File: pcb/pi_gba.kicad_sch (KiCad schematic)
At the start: 22 parts, among them SW1 EG1206A, SW10 L1, SW11 R1, SW12 Start, SW13 Select, SW14 L2, SW15 R2, SW16 Menu, SW2 Left, SW3 Down, SW4 Up, SW5 Right, SW6 Y, SW7 X, SW8 B, SW9 A, U1 RPI_Zero2W, U2 ER-TFTM035-6, U3 Powerboost_1000C

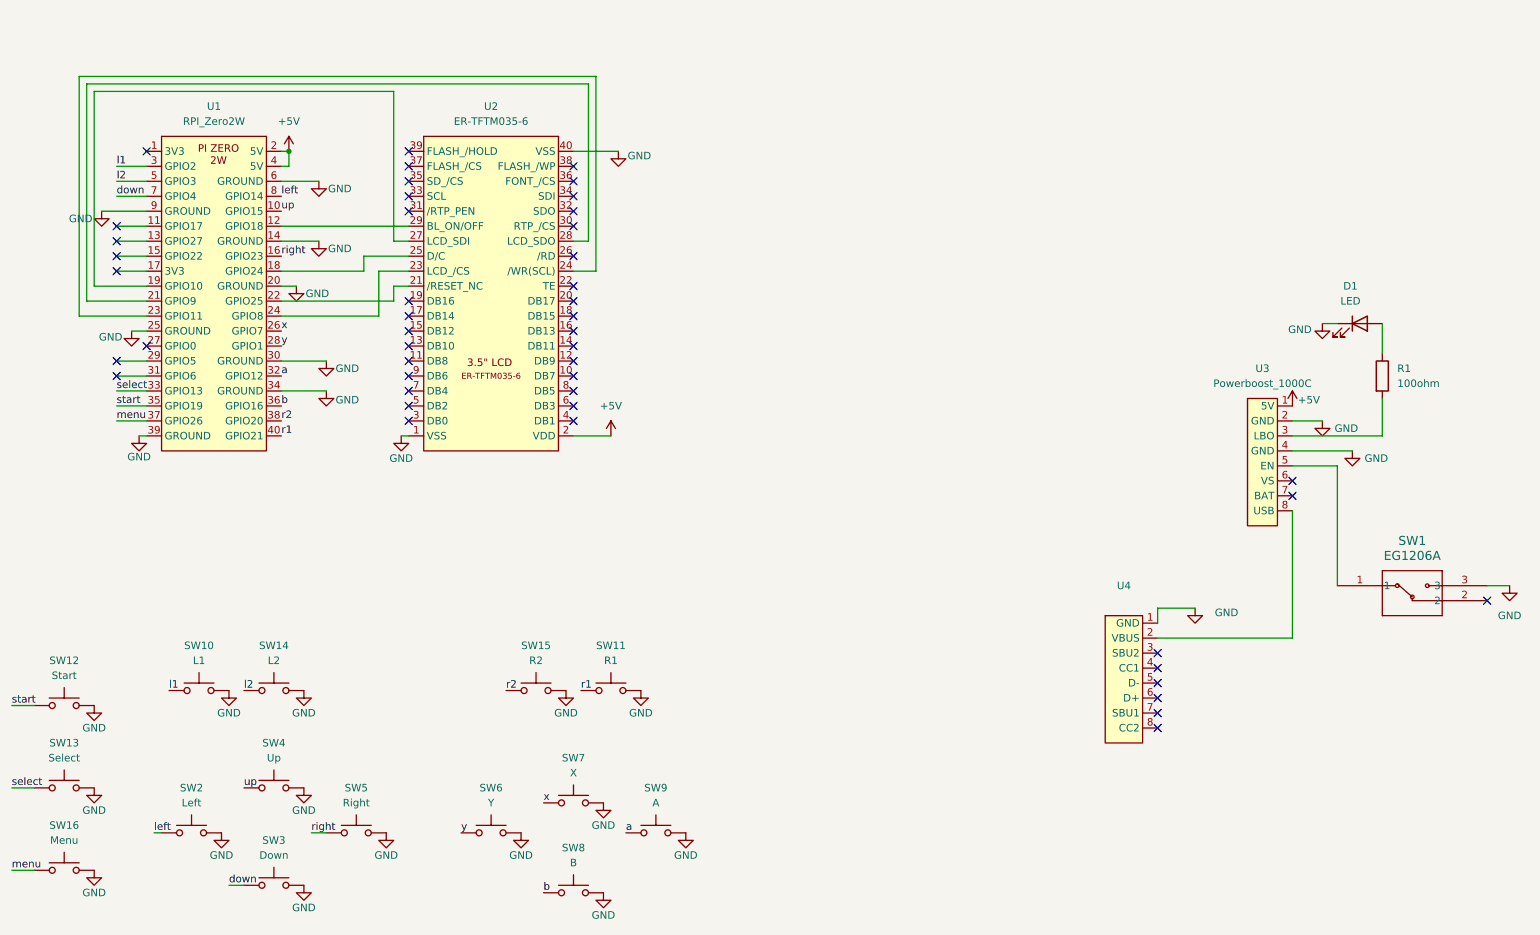
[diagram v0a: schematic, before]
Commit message: schematic redesign
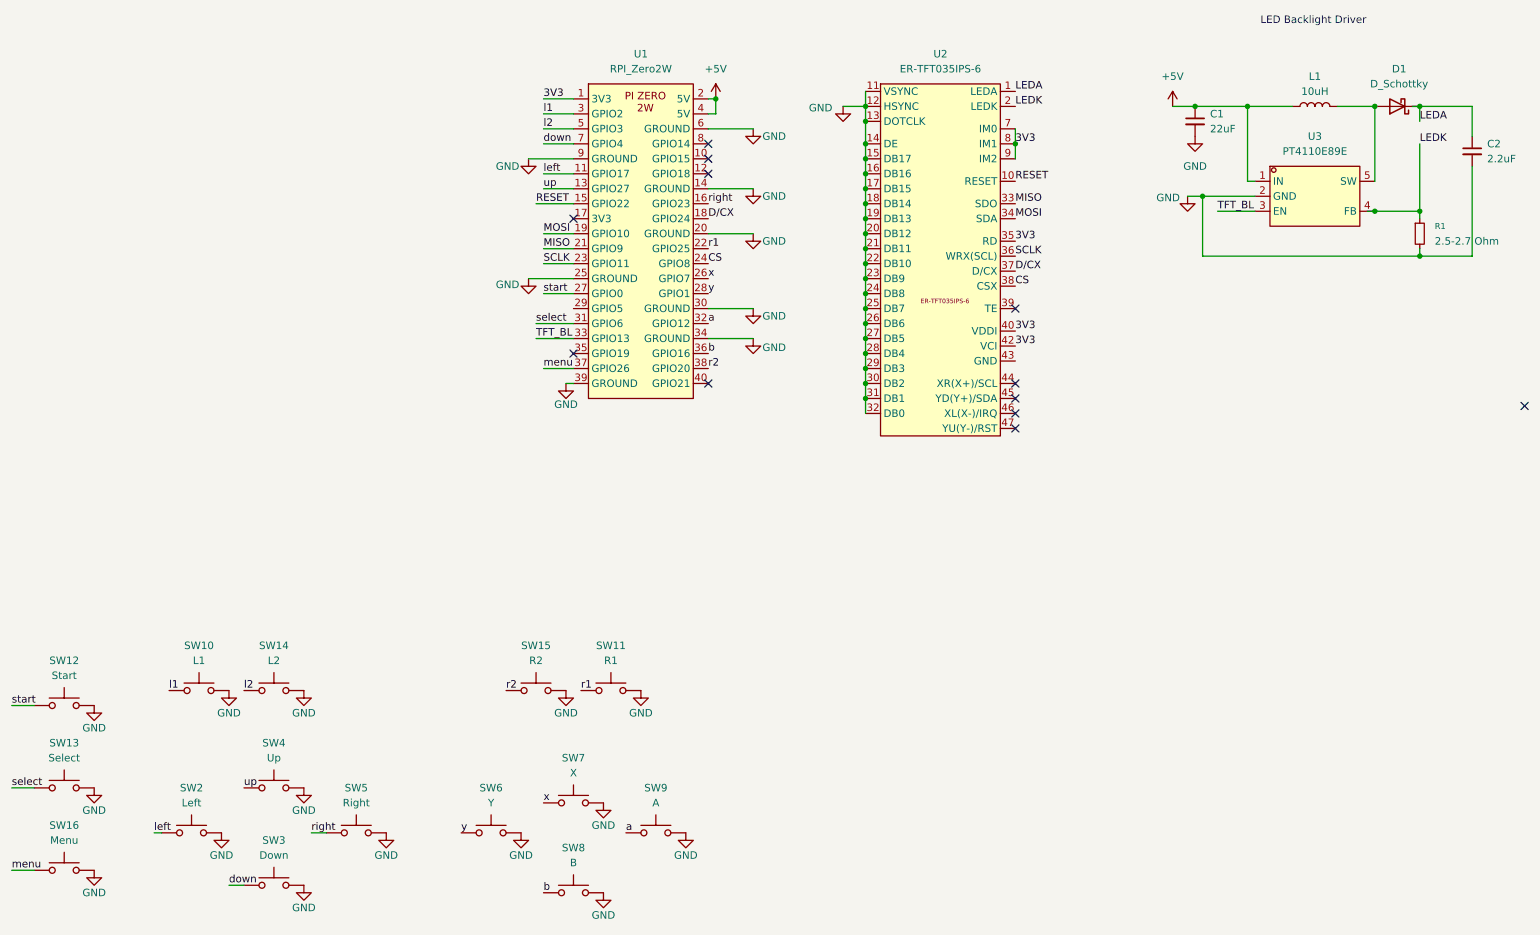
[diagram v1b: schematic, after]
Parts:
- removed D1: LED, LED_THT:LED_D5.0mm, symbol Device:LED
- removed R1: 100ohm, Resistor_THT:R_Axial_DIN0207_L6.3mm_D2.5mm_P10.16mm_Horizontal, symbol Device:R
- removed SW1: EG1206A, pi_gba_footprints:EG1206A_EWI, symbol switch:EG1206A
- removed U2: ER-TFTM035-6, pi_gba_footprints:ER-TFTM035-6, symbol pi_gba:ER-TFTM035-6
- removed U3: Powerboost_1000C, pi_gba_footprints:adafruit_powerboost_1000c, symbol pi_gba:adafruit_powerboost_1000c
- removed U4: ~, pi_gba_footprints:adafruit_usbc_breakout, symbol pi_gba:adafruit_usbc_breakout
- added C1: 22uF, symbol Device:C_Small
- added C2: 2.2uF, symbol Device:C_Small
- added D1: D_Schottky, symbol Device:D_Schottky
- added L1: 10uH, symbol Device:L
- added R1: 2.5-2.7 Ohm, symbol Device:R_Small
- added U2: ER-TFT035IPS-6, symbol pi_gba:ER-TFT035IPS-6
- added U3: PT4110E89E, easyeda2kicad:SOT-89-5_L4.5-W2.5-P1.50-LS4.5-BR, symbol easyeda2kicad:PT4110E89E
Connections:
- net +5V: now also C1.1, L1.1, U3.1 (IN)
- net GND: now also C1.2, C2.2, R1.2, U2.11 (VSYNC), U2.12 (HSYNC), U2.13 (DOTCLK), U2.14 (DE), U2.15 (DB17), U2.16 (DB16), U2.17 (DB15), U2.18 (DB14), U2.19 (DB13), U2.20 (DB12), U2.21 (DB11), U2.22 (DB10), U2.23 (DB9), U2.24 (DB8), U2.25 (DB7), U2.26 (DB6), U2.27 (DB5), U2.28 (DB4), U2.29 (DB3), U2.30 (DB2), U2.31 (DB1), U2.32 (DB0), U2.43 (GND), U2.48 (GND), U2.49 (GND), U2.50 (GND), U3.2 (GND)
- net left: now also U1.11 (GPIO17); no longer U1.8 (GPIO14)
- net r1: now also U1.22 (GPIO25); no longer U1.40 (GPIO21)
- net select: now also U1.31 (GPIO6); no longer U1.33 (GPIO13)
- net start: now also U1.27 (GPIO0); no longer U1.35 (GPIO19)
- net up: now also U1.13 (GPIO27); no longer U1.10 (GPIO15)
- net CS: now reaches U1.24 (GPIO8)
- net CS: now also U2.38 (CSX)
- net SCLK: now reaches U1.23 (GPIO11)
- net SCLK: now also U2.36 (WRX(SCL))
- net D/CX: now reaches U1.18 (GPIO24)
- net D/CX: now also U2.37 (D/CX)
- net MOSI: now reaches U1.19 (GPIO10)
- net MOSI: now also U2.34 (SDA)
- net MISO: now reaches U1.21 (GPIO9)
- net MISO: now also U2.33 (SDO)
- net VDDI: now reaches U1.1 (3V3)
- net VDDI: now also U2.35 (RD), U2.40 (VDDI), U2.41 (VDDI), U2.42 (VCI), U2.7 (IM0), U2.8 (IM1), U2.9 (IM2)
- net RESET: now reaches U1.15 (GPIO22)
- net RESET: now also U2.10 (RESET)
- new net: U2.4 (NC), U2.5 (NC), U2.6 (NC)
- new net: D1.2 (A), L1.2, U3.5 (SW)
- new net LEDA: C2.1, D1.1 (K), U2.1 (LEDA)
- new net LEDK: R1.1, U2.2 (LEDK), U2.3 (LEDK), U3.4 (FB)
- new net TFT_BL: U1.33 (GPIO13), U3.3 (EN)
- no-connect marks 47 -> 12
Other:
- note added: "LED Backlight Driver"
- moved on the sheet: U1
